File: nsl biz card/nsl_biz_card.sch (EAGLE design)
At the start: 3 parts, among them U2 ATMEGA328P-AU

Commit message: NSL biz card!
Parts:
- removed U2: ATMEGA328P-AU, Ava:ATMEGA328P-AU
- added BAT1: (no value), SparkFun:BATTERY12MM
- added C1, C2, C4: 15pF, SparkFun:CAP0603-CAP
- added C10, C11, C12: 4.7uF, SparkFun:CAP0603-CAP
- added C13, C14: (no value), badge.lbrbadge_2013:SPARKFUN_CAP0603-CAP
- added C15, C16, C17, C18: 0.1uF, badge.lbrbadge_2013:SPARKFUN_CAP0603-CAP
- added C19: 1uF, badge.lbrbadge_2013:SPARKFUN_CAP0603-CAP
- added C3: 8.2pF, SparkFun:CAP0603-CAP
- added C5: 33pF, SparkFun:CAP0603-CAP
- added C6: 100nF, SparkFun:CAP0603-CAP
- added C7: 10uF, SparkFun:CAP0603-CAP
- added C8, C9: 1uF, SparkFun:CAP0603-CAP
- added D1: USBUG_PRTR5V0U2X, badge.lbrbadge_2013:USBUG_PRTR5V0U2X
- added IC1: (no value), badge.lbrbadge_2013:OUTLINE_NONOLITH_ATXMEGAXXA4U-AU
- added J$1: SMA_EDGE, SparkFun:SMA_EDGE
- added JP1: (no value), SparkFun:M06SIP
- added JP2: (no value), badge.lbrbadge_2013:MICROBUILDER_HEADER-1X2
- added JP3: DASPILKER_USB-RECEPTABLE-HIROSE-ZX62-AB-5PA(11), badge.lbrbadge_2013:DASPILKER_USB-RECEPTABLE-HIROSE-ZX62-AB-5PA(11)
- added L1, L2: 18nH, SparkFun:INDUCTOR0603
- added L3: 56nH, SparkFun:INDUCTOR0603
- added L4: 220nH, SparkFun:INDUCTOR0603
- added LED1, LED2, LED3: (no value), badge.lbrbadge_2013:LED_LEDCHIP-LED0805
- added R1: 100k, SparkFun:RESISTOR0603-RES
- added R2: 820K, SparkFun:RESISTOR0603-RES
- added S1, S2, S3, S4: SWITCH-MOMENTARY-2, SparkFun:SWITCH-MOMENTARY-2
- added SJ1: (no value), badge.lbrbadge_2013:MICROBUILDER_SOLDERJUMPERREFLOW
- added U$3: CRYSTAL_3.2X2.5-TCXO, picoAVA-R8:CRYSTAL_3.2X2.5-TCXO
- added U$4: SPARKFUN_AP7333-33SOT23-3, badge.lbrbadge_2013:SPARKFUN_AP7333-33SOT23-3
- added X1: M6-RF315_NX3225GA, badge.lbrbadge_2013:M6-RF315_NX3225GA
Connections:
- new net +5V: D1.P$3, JP3.VCC, U$4.IN
- new net ANTENNA: SJ1.1
- new net BT1: IC1.PA1/ADC1, S4.2
- new net BT2: IC1.PA2/ADC2, S3.2
- new net BT3: IC1.PA3/ADC3, S2.2
- new net BT4: IC1.PA4/ADC4, S1.2
- new net D+: D1.P$4, IC1.TXD1/USB+/PD7, JP3.D+
- new net D-: D1.P$2, IC1.RXD1/MISO/USB-/PD6, JP3.D-
- new net D/C: IC1.PB3/ADC11/DAC1, U1.DC/I2C_SA0
- new net DAT: IC1.PDI-DATA, JP2.1
- new net DISP_CS: IC1.PB0/ADC8/AREFB, U1./CS
- new net GND: BAT1.-, C10.2, C11.2, C12.2, C13.1, C14.1, C15.2, C16.2, C17.2, C18.2, C19.2, C2.2, C3.2, C5.2, C6.2, C7.2, D1.P$1, IC1.GND@1, IC1.GND@2, IC1.GND@3, IC1.GND@4, J$1.GND@0, J$1.GND@1, J$1.GND@2, J$1.GND@3, JP1.1, JP1.2, JP3.GND, LED1.C, LED2.C, LED3.C, R1.2, R2.1, S1.1, S2.1, S3.1, S4.1, U$1.GND, U$1.GND2, U$3.GND, U$3.TRI, U$4.GND, U1.BS0, U1.BS1, U1.BS2, U1.NC(GND)@1, U1.NC(GND)@2, U1.VLSS, U1.VSS
- new net GPIO0: U$1.GPIO0
- new net GPIO1: U$1.GPIO1
- new net LNK: IC1.XCK0/OC0B/SCL/PE1, JP1.6
- new net MISO: IC1.PC6/MISO/RXD1, U$1.SDO
- new net MOSI: IC1.PC5/OC1B/MOSI/XCK1, U$1.SDI
- new net N$10: IC1.PA6/ADC6, LED2.A
- new net N$11: IC1.PA5/ADC5, LED1.A
- new net N$12: C12.1, U1.VCC
- new net N$13: IC1.RESET/PDI-CLK, JP2.2
- new net N$14: C9.1, U1.C2P
- new net N$15: C9.2, U1.C2N
- new net N$16: C8.1, U1.C1P
- new net N$17: C8.2, U1.C1N
- new net N$18: C11.1, U1.VCOMH
- new net N$19: R2.2, U1.IREF
- new net N$2: C1.1, U$3.OUT
- new net N$20: J$1.SIGNAL, L1.1, SJ1.2
- new net N$3: C4.2, L4.2, U$1.TX
- new net N$4: C4.1, L3.2
- new net N$5: C3.1, L2.2, L3.1
- new net N$6: C2.1, L1.2, L2.1
- new net N$7: C13.2, IC1.PR0/XTAL2, X1.2
- new net N$8: IC1.PA7/ADC7, LED3.A
- new net N$9: C14.2, IC1.PR1/XTAL1, X1.1
- new net RES: IC1.PB1/ADC9, U1./RES
- new net RF_SEL: IC1.PC4/OC1A/#SS, U$1.NSEL
- new net RX: IC1.RXD0/OC0C/PE2, JP1.4
- new net SCK: IC1.PC7/SCK/TXD1/CLKO/EVO, U$1.SCLK
- new net SCL: IC1.PC1/OC0B/XCK0/SCL
- new net SCLK/DB0: IC1.OC0B/XCK0/PD1, U1.D0/SPI_SCLK/I2C_SCK
- new net SDA: IC1.PC0/OC0A/SDA
- new net SDIN/DB1: IC1.OC0D/TXD0/PD3, U1.D1/SPI_SDIN/I2C_SDA
- new net SHUTDOWN: IC1.PB2/ADC10/DAC0, R1.1, U$1.SDN
- new net TX: IC1.TXD0/OC0D/PE3, JP1.5
- new net VCC: C10.1, C15.1, C16.1, C17.1, C18.1, C19.1, C5.1, C6.1, C7.1, IC1.AVCC, IC1.VCC@1, IC1.VCC@2, IC1.VCC@3, JP1.3, L4.1, U$1.VDD, U$1.VDD2, U$3.VDD, U$4.OUT, U1.VBAT, U1.VDD
- new net XIN: C1.2, U$1.XIN
- new net XOUT: U$1.XOUT

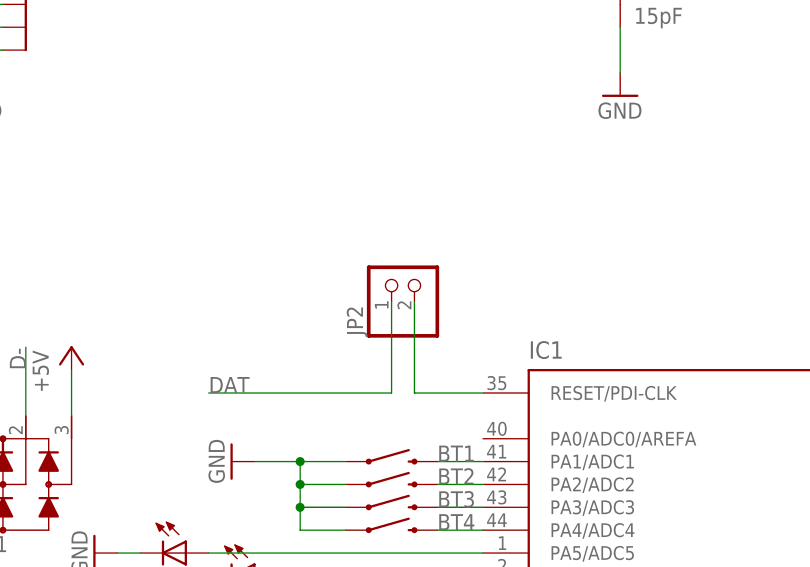
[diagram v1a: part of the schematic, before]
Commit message: updated programming header
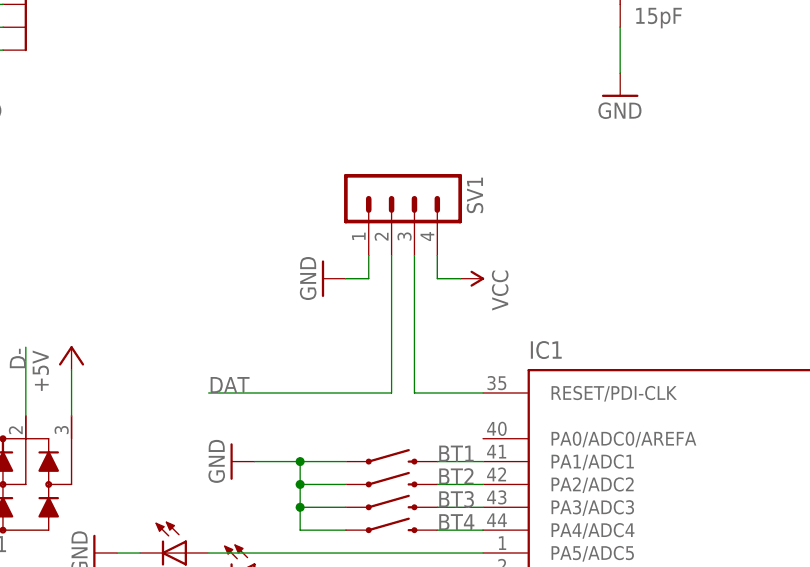
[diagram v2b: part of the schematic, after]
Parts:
- removed JP2: (no value), badge.lbrbadge_2013:MICROBUILDER_HEADER-1X2
- added SV1: (no value), con-lstb:MA04-1
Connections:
- net DAT: now also SV1.2; no longer JP2.1
- net GND: now also SV1.1
- net N$13: now also SV1.3; no longer JP2.2
- net VCC: now also SV1.4
